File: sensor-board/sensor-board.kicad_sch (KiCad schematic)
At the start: 12 parts, among them J1 Batt, Q1 DMG3415U-7, U1 MCP73831-3-OT, U2 Arduino-nano-BLE-33, U3 SCD40-D-R2, U4 SGP40-D-R4

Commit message: update sensors and sensorBoard
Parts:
- removed U3: SCD40-D-R2, hack-it-back:SCD40DR2, symbol hack-it-back:SCD40-D-R2
- added C3, C4, C5: 10uF, Capacitor_SMD:C_0805_2012Metric, symbol Device:C_Small
- added C6: 1uF, Capacitor_SMD:C_0805_2012Metric, symbol Device:C_Small
- added J2: I2C, Connector_PinHeader_2.54mm:PinHeader_1x04_P2.54mm_Vertical, symbol Connector_Generic:Conn_01x04
- added R4: 4.7R, Resistor_SMD:R_0805_2012Metric, symbol Device:R_Small
- added U3: MCP1700T-3102, Package_TO_SOT_SMD:SOT-23, symbol Regulator_Linear:MCP1700-3302E_SOT23
- J1: footprint (none) -> Connector_PinHeader_2.54mm:PinHeader_1x02_P2.54mm_Vertical
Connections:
- net +BATT: now also C4.1
- net GND: now also U2.19, U4.2 (VSS), U4.4 (N/A), U4.7 (EP), C3.2, C4.2, C5.2, C6.2, J2.4 (Pin_4), U3.1 (GND)
- net VBUS: now also C3.1
- net VDD: now also U3.3 (VI); no longer U2.15
- net at U4.1 (VDD): now also U4.5 (VDDH), C6.1, R4.1
- net SDA: now reaches U4.3 (SDA)
- net SDA: now also J2.2 (Pin_2)
- net SCL: now reaches U4.6 (SCL)
- net SCL: now also J2.3 (Pin_3)
- net +3V3: now reaches U2.2
- net +3V3: now also C5.1, J2.1 (Pin_1), R4.2, U3.2 (VO)
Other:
- note added: "If Vbus active +Batt disconnected from Regulator"
- note removed: "If Vbus active +Batt disconnected from Vin"
- moved on the sheet: U2, U4

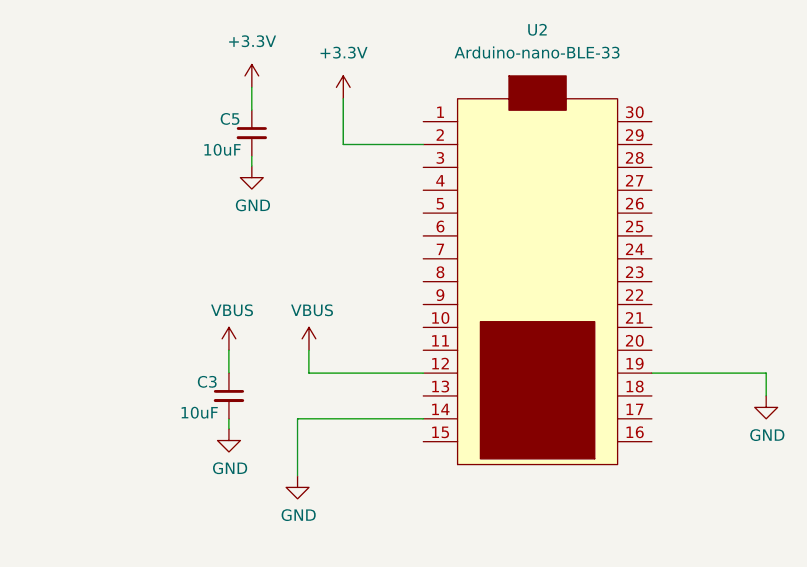
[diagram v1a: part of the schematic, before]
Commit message: update pins sensor board
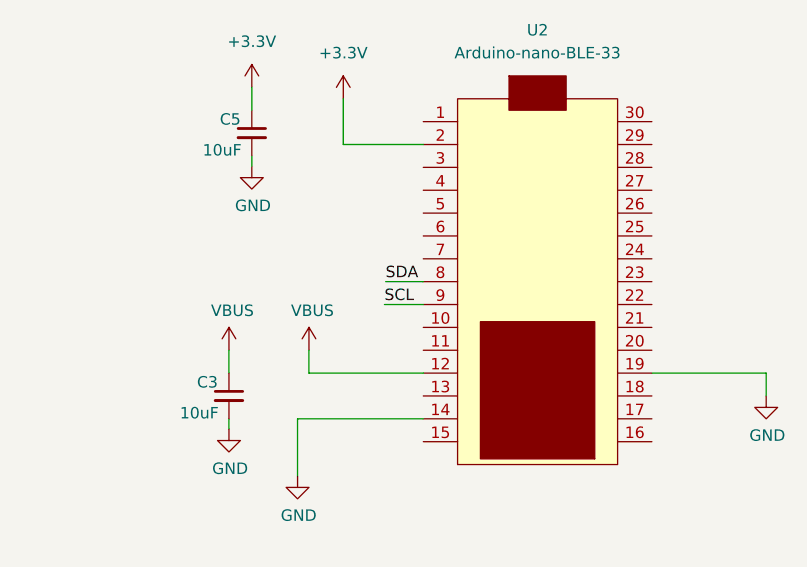
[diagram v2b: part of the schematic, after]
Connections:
- net SCL: now also U2.9
- net SDA: now also U2.8
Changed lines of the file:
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@@
+    (stroke (width 0) (type default) (color 0 0 0 0))
+  )
+  (wire (pts (xy 179.832 46.9392) (xy 184.023 46.9392))
     (stroke (width 0) (type default) (color 0 0 0 0))
   )
@@
     (stroke (width 0) (type default) (color 0 0 0 0))
   )
+  (wire (pts (xy 179.705 49.4792) (xy 184.023 49.4792))
+    (stroke (width 0) (type default) (color 0 0 0 0))
+  )
   (wire (pts (xy 57.658 26.797) (xy 57.658 20.828))
     (stroke (width 0) (type default) (color 0 0 0 0))
@@
     (effects (font (size 1.27 1.27)) (justify left bottom))
   )
+  (label "SDA" (at 179.832 46.9392 0)
+    (effects (font (size 1.27 1.27)) (justify left bottom))
+  )
   (label "SDA" (at 110.3122 71.9328 0)
     (effects (font (size 1.27 1.27)) (justify left bottom))
   )
+  (label "SCL" (at 179.705 49.4792 0)
+    (effects (font (size 1.27 1.27)) (justify left bottom))
+  )

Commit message: update sensor board v1.0
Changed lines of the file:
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@@
   )
   (symbol (lib_id "power:+3.3V") (at 168.5544 94.5134 0) (unit 1)
-    (in_bom yes) (on_board yes) (fields_autoplaced)
+    (in_bom yes) (on_board yes)
     (property "Reference" "#PWR012" (id 0) (at 168.5544 98.3234 0)
       (effects (font (size 1.27 1.27)) hide)
     )
-    (property "Value" "+3.3V" (id 1) (at 168.5544 89.4334 0))
+    (property "Value" "+3.3V" (id 1) (at 168.0972 88.9254 0))
     (property "Footprint" "" (id 2) (at 168.5544 94.5134 0)
       (effects (font (size 1.27 1.27)) hide)
